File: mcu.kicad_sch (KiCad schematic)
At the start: 17 parts, among them J2 SWD_HIL, U8 STM32G431RBT6

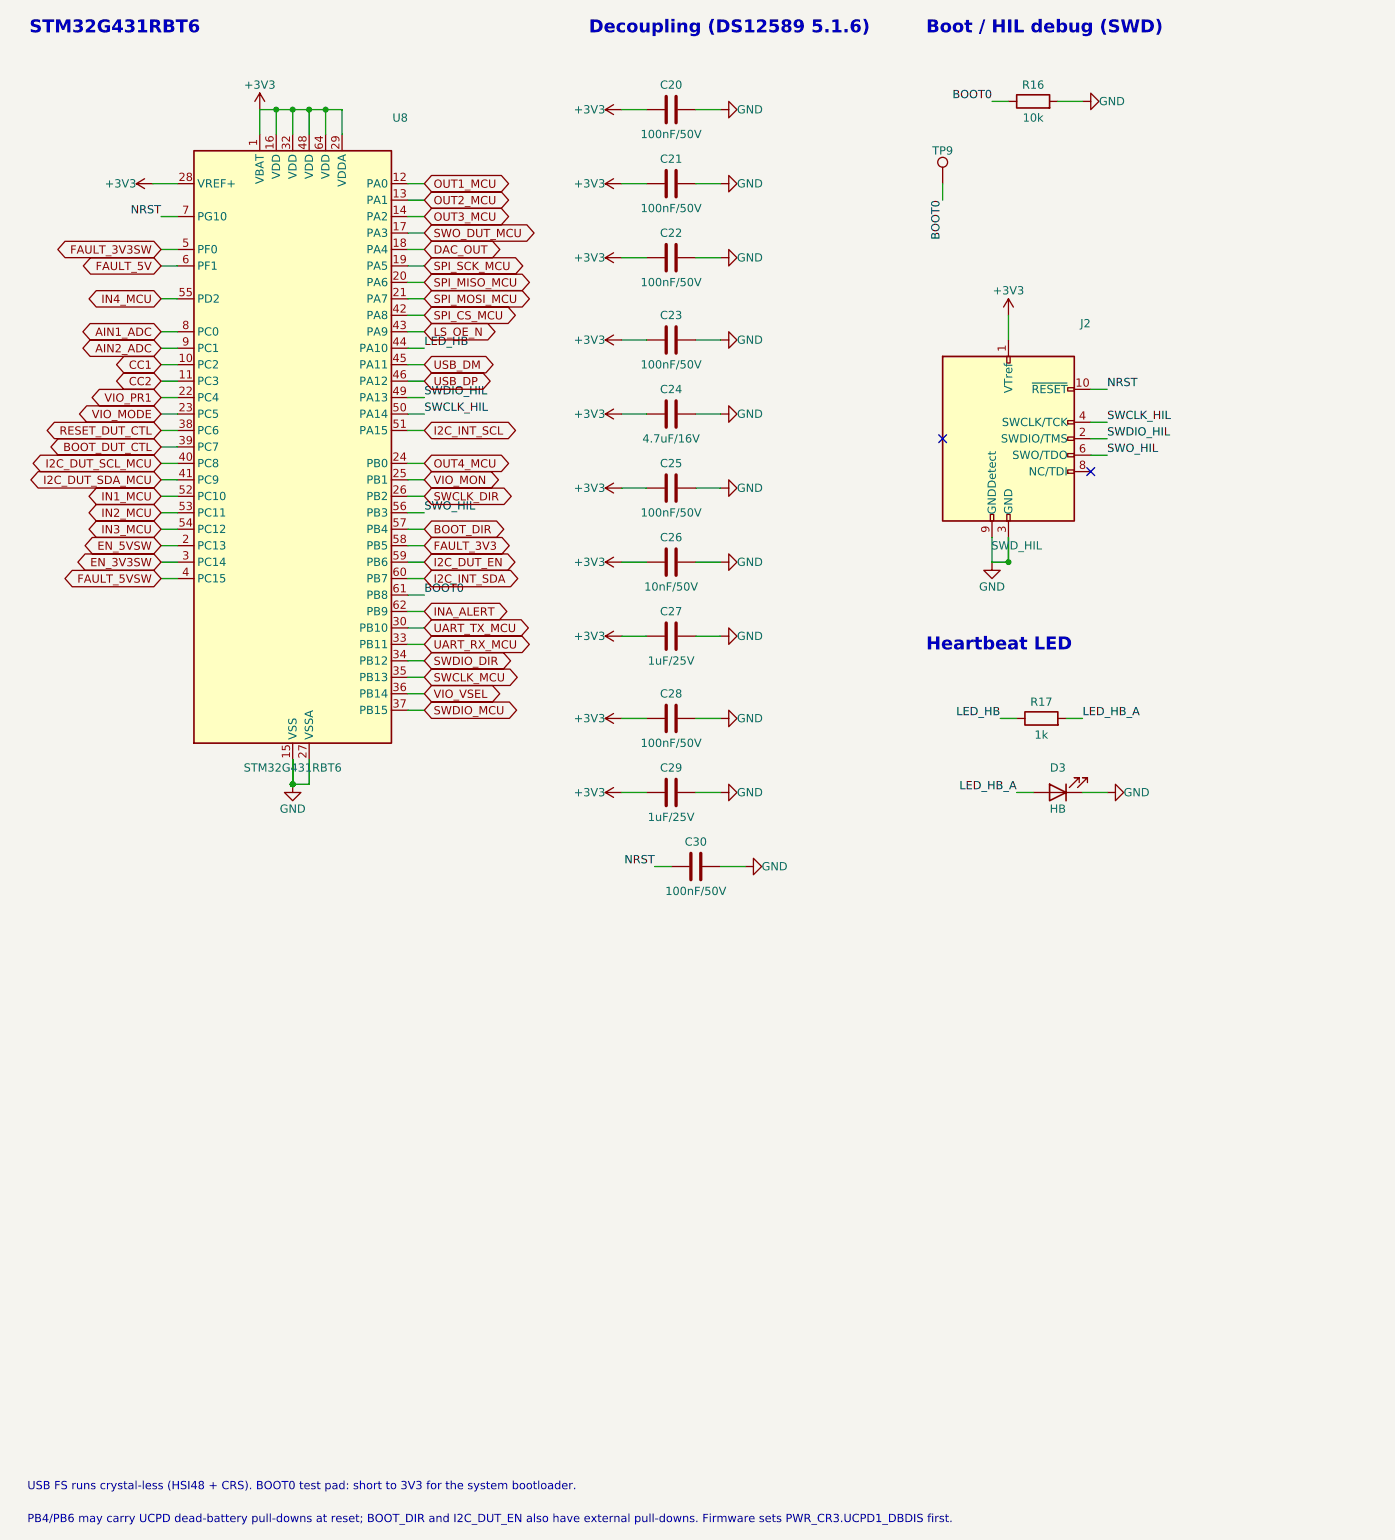
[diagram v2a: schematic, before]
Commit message: fix: apply schematic review (LQFP-80 MCU, fixed-rail EN, VIO from 5V_DUT, buttons, ESD per header)
- STM32G431MBT6 (LQFP-80): 14 more GPIO; BOOT_DIR off PB4 (JTRST pull-up at reset)
- Fixed DUT rails: EN on PE7/PE8 with pull-up (on by default, firmware can cut)
- TPS2116 VIN1 from current-limited 5V_DUT instead of +5V
- Two user push buttons (TS-1187A) on PD0/PD1, BOOT0 solder jumper
- TVS after the PTC, buck Cin 10uF/25V 0805, 5th VDD decoupling cap
- No floating translator inputs (U15 A8 to GND, 1M bias on U14 B side)
- ESD channels grouped per header; datasheet field falls back to LCSC page
- Decoupling capacitors declare the pin they decouple (validated against nets)

Co-Authored-By: Claude Opus 5.5 <noreply@anthropic.com>
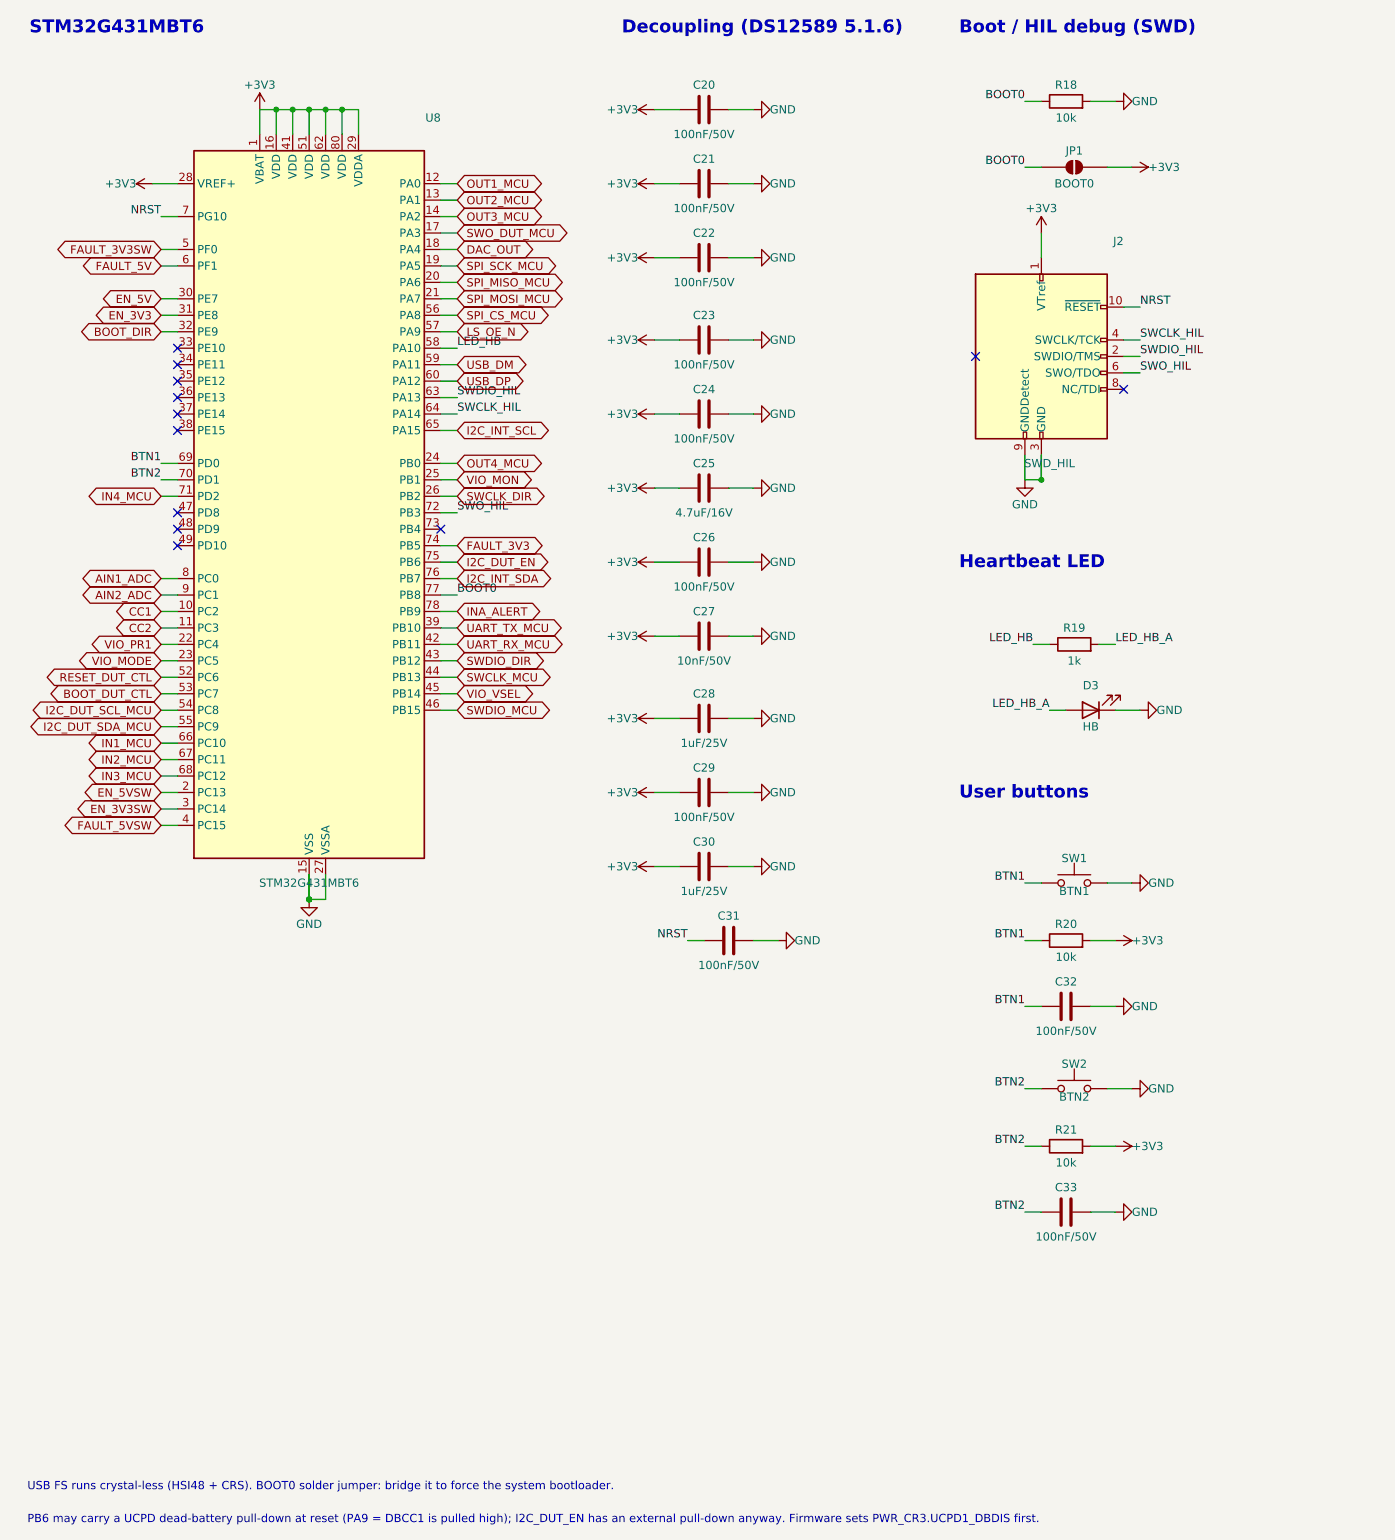
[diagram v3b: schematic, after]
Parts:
- removed R16: 10k, Resistor_SMD:R_0402_1005Metric, symbol Device:R
- removed R17: 1k, Resistor_SMD:R_0402_1005Metric, symbol Device:R
- removed TP9: BOOT0, TestPoint:TestPoint_Pad_D1.5mm, symbol Connector:TestPoint
- added C31, C32, C33: 100nF/50V, Capacitor_SMD:C_0402_1005Metric, symbol Device:C
- added JP1: BOOT0, Jumper:SolderJumper-2_P1.3mm_Open_RoundedPad1.0x1.5mm, symbol Jumper:SolderJumper_2_Open
- added R18, R20, R21: 10k, Resistor_SMD:R_0402_1005Metric, symbol Device:R
- added R19: 1k, Resistor_SMD:R_0402_1005Metric, symbol Device:R
- added SW1: BTN1, Button_Switch_SMD:SW_Push_1P1T_XKB_TS-1187A, symbol Switch:SW_Push
- added SW2: BTN2, Button_Switch_SMD:SW_Push_1P1T_XKB_TS-1187A, symbol Switch:SW_Push
- C24: value 4.7uF/16V -> 100nF/50V; footprint Capacitor_SMD:C_0603_1608Metric -> Capacitor_SMD:C_0402_1005Metric; LCSC C19666 -> C307331; MPN CL10A475KO8NNNC -> CL05B104KB54PNC
- C25: value 100nF/50V -> 4.7uF/16V; footprint Capacitor_SMD:C_0402_1005Metric -> Capacitor_SMD:C_0603_1608Metric; LCSC C307331 -> C19666; MPN CL05B104KB54PNC -> CL10A475KO8NNNC
- C26: value 10nF/50V -> 100nF/50V; LCSC C15195 -> C307331; MPN CL05B103KB5NNNC -> CL05B104KB54PNC
- C27: value 1uF/25V -> 10nF/50V; LCSC C52923 -> C15195; MPN CL05A105KA5NQNC -> CL05B103KB5NNNC
- C28, C30: value 100nF/50V -> 1uF/25V; LCSC C307331 -> C52923; MPN CL05B104KB54PNC -> CL05A105KA5NQNC
- C29: value 1uF/25V -> 100nF/50V; LCSC C52923 -> C307331; MPN CL05A105KA5NQNC -> CL05B104KB54PNC
- U8: value STM32G431RBT6 -> STM32G431MBT6; footprint Package_QFP:LQFP-64_10x10mm_P0.5mm -> Package_QFP:LQFP-80_12x12mm_P0.5mm; symbol MCU_ST_STM32G4:STM32G431RBTx -> MCU_ST_STM32G4:STM32G431MBTx; LCSC C431633 -> C730099; MPN STM32G431RBT6 -> STM32G431MBT6
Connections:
- net +3V3: now also C30.1, U8.41 (VDD), U8.51 (VDD), U8.62 (VDD), U8.80 (VDD), JP1.2 (B), R20.2, R21.2; no longer U8.32 (VDD), U8.48 (VDD), U8.64 (VDD)
- net BOOT0: now also U8.77 (PB8), JP1.1 (A), R18.1; no longer U8.61 (PB8)
- net BOOT_DIR: now also U8.32 (PE9); no longer U8.57 (PB4)
- net BOOT_DUT_CTL: now also U8.53 (PC7); no longer U8.39 (PC7)
- net FAULT_3V3: now also U8.74 (PB5); no longer U8.58 (PB5)
- net GND: now also U8.40 (VSS), U8.50 (VSS), U8.61 (VSS), U8.79 (VSS), C31.2, C32.2, C33.2, R18.2, SW1.2, SW2.2; no longer U8.31 (VSS), U8.47 (VSS), U8.63 (VSS)
- net I2C_DUT_EN: now also U8.75 (PB6); no longer U8.59 (PB6)
- net I2C_DUT_SCL_MCU: now also U8.54 (PC8); no longer U8.40 (PC8)
- net I2C_DUT_SDA_MCU: now also U8.55 (PC9); no longer U8.41 (PC9)
- net I2C_INT_SCL: now also U8.65 (PA15); no longer U8.51 (PA15)
- net I2C_INT_SDA: now also U8.76 (PB7); no longer U8.60 (PB7)
- net IN1_MCU: now also U8.66 (PC10); no longer U8.52 (PC10)
- net IN2_MCU: now also U8.67 (PC11); no longer U8.53 (PC11)
- net IN3_MCU: now also U8.68 (PC12); no longer U8.54 (PC12)
- net IN4_MCU: now also U8.71 (PD2); no longer U8.55 (PD2)
- net INA_ALERT: now also U8.78 (PB9); no longer U8.62 (PB9)
- net LED_HB: now also U8.58 (PA10), R19.1; no longer U8.44 (PA10)
- net LED_HB_A: now also R19.2
- net LS_OE_N: now also U8.57 (PA9); no longer U8.43 (PA9)
- net NRST: now also C31.1; no longer C30.1
- net RESET_DUT_CTL: now also U8.52 (PC6); no longer U8.38 (PC6)
- net SPI_CS_MCU: now also U8.56 (PA8); no longer U8.42 (PA8)
- net SWCLK_HIL: now also U8.64 (PA14); no longer U8.50 (PA14)
- net SWCLK_MCU: now also U8.44 (PB13); no longer U8.35 (PB13)
- net SWDIO_DIR: now also U8.43 (PB12); no longer U8.34 (PB12)
- net SWDIO_HIL: now also U8.63 (PA13); no longer U8.49 (PA13)
- net SWDIO_MCU: now also U8.46 (PB15); no longer U8.37 (PB15)
- net SWO_HIL: now also U8.72 (PB3); no longer U8.56 (PB3)
- net UART_RX_MCU: now also U8.42 (PB11); no longer U8.33 (PB11)
- net UART_TX_MCU: now also U8.39 (PB10); no longer U8.30 (PB10)
- net USB_DM: now also U8.59 (PA11); no longer U8.45 (PA11)
- net USB_DP: now also U8.60 (PA12); no longer U8.46 (PA12)
- net VIO_VSEL: now also U8.45 (PB14); no longer U8.36 (PB14)
- new net BTN1: C32.1, R20.1, SW1.1, U8.69 (PD0)
- new net BTN2: C33.1, R21.1, SW2.1, U8.70 (PD1)
- new net EN_3V3: U8.31 (PE8)
- new net EN_5V: U8.30 (PE7)
- no-connect marks 2 -> 12
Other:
- note added: "PB6 may carry a UCPD dead-battery pull-down at reset (PA9 = DBCC1 is pulled high); I2C_DUT_EN has an external pull-down anyway. Firmware sets PWR_CR3.UCPD1_DBDIS first."
- note added: "STM32G431MBT6"
- note added: "USB FS runs crystal-less (HSI48 + CRS). BOOT0 solder jumper: bridge it to force the system bootloader."
- note added: "User buttons"
- note removed: "PB4/PB6 may carry UCPD dead-battery pull-downs at reset; BOOT_DIR and I2C_DUT_EN also have external pull-downs. Firmware sets PWR_CR3.UCPD1_DBDIS first."
- note removed: "STM32G431RBT6"
- note removed: "USB FS runs crystal-less (HSI48 + CRS). BOOT0 test pad: short to 3V3 for the system bootloader."
- title: MCU STM32G431RBT6 -> MCU STM32G431MBT6
- moved on the sheet: C20, C21, C22, C23, C24, C25, C26, C27, C28, C29, C30, D3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

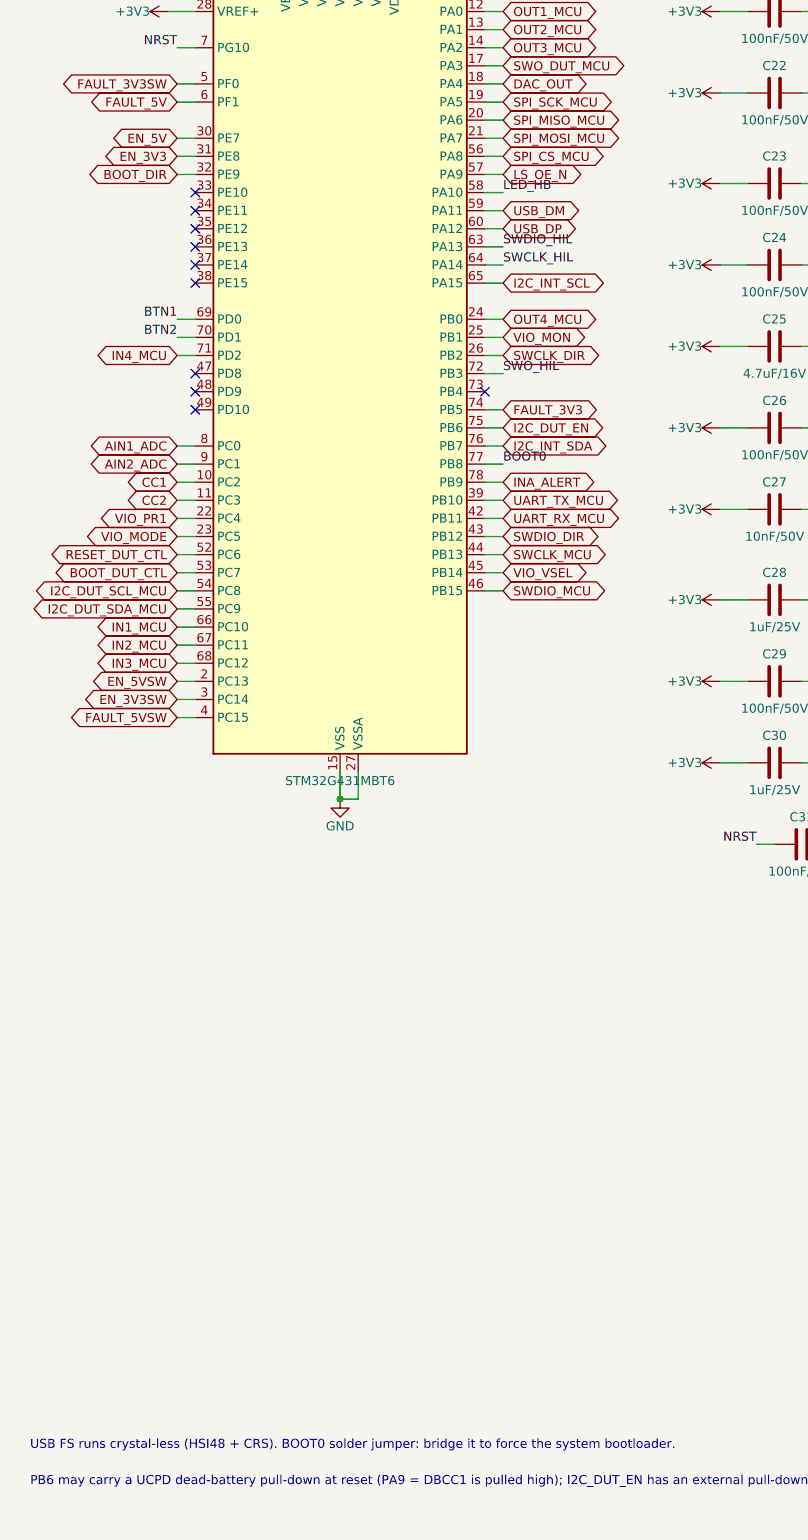
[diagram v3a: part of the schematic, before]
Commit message: fix: assign MCU pins to the PCB floor plan, drop test points duplicated by headers
- EN_5V/EN_3V3 on PD8/PD9 and BOOT_DIR on PD10 (pins facing the power and debug blocks)
- BTN1/BTN2 on PE11/PE10 and LED_HB on PE12 (pins facing the top-right corner)
- Second buck output capacitor declared next to the first one
- DUT rail and VIO test points removed: J_PWR / J_DBG pins expose those nets

Co-Authored-By: Claude Opus 5.5 <noreply@anthropic.com>
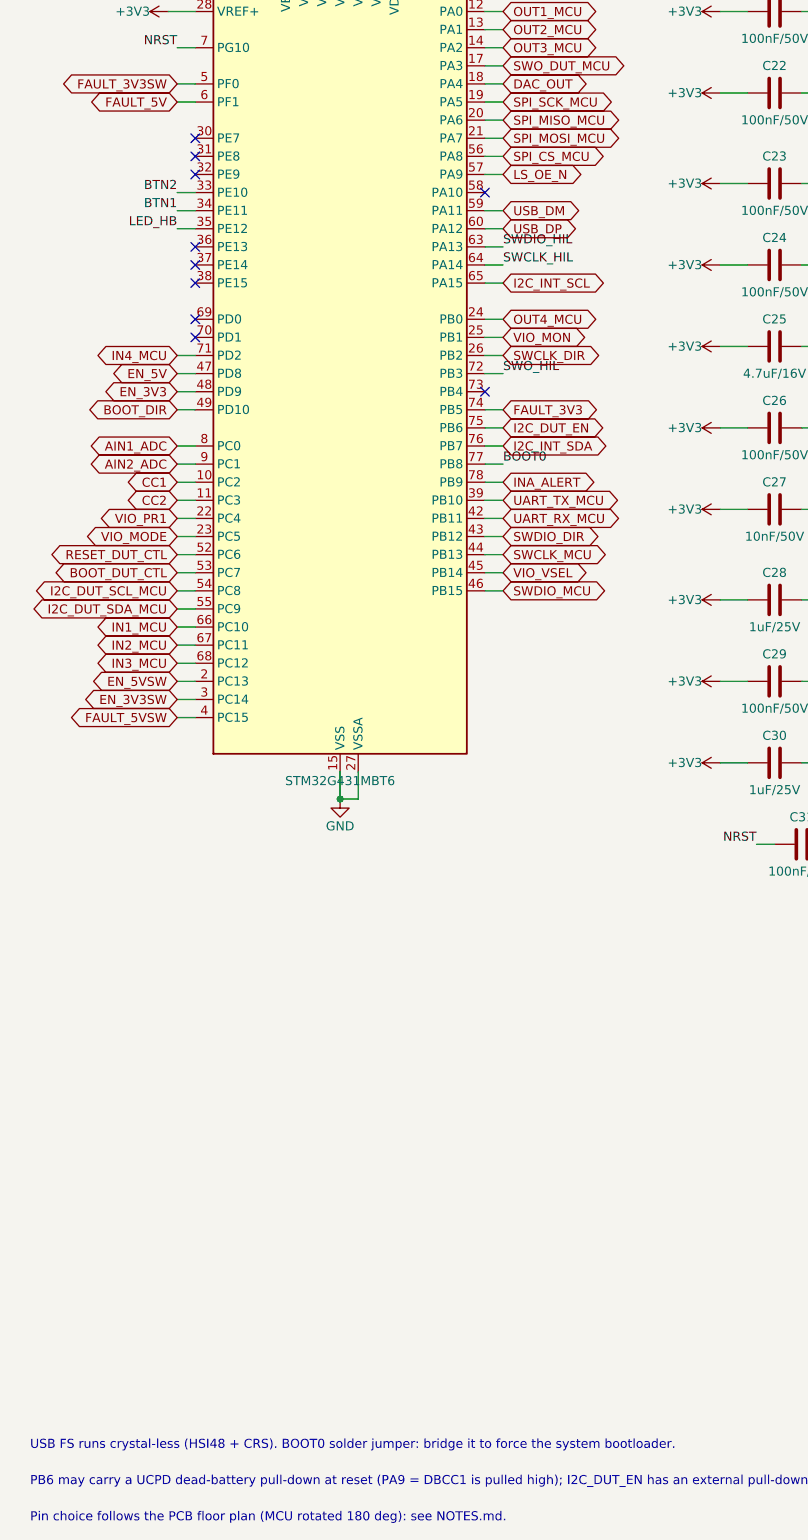
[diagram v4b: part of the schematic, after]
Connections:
- net BOOT_DIR: now also U8.49 (PD10); no longer U8.32 (PE9)
- net BTN1: now also U8.34 (PE11); no longer U8.69 (PD0)
- net BTN2: now also U8.33 (PE10); no longer U8.70 (PD1)
- net EN_3V3: now also U8.48 (PD9); no longer U8.31 (PE8)
- net EN_5V: now also U8.47 (PD8); no longer U8.30 (PE7)
- net LED_HB: now also U8.35 (PE12); no longer U8.58 (PA10)
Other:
- note added: "Pin choice follows the PCB floor plan (MCU rotated 180 deg): see NOTES.md."
